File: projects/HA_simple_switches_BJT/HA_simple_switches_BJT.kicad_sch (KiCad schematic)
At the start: 16 parts

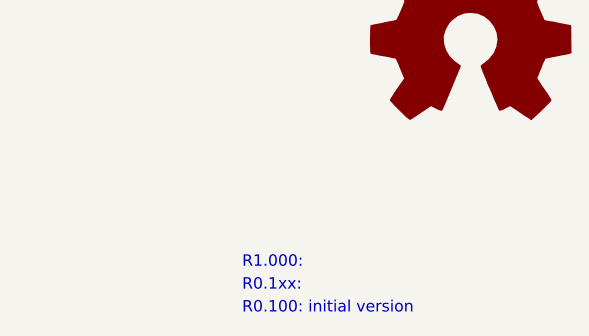
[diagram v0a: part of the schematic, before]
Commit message: v101 minor routing changes
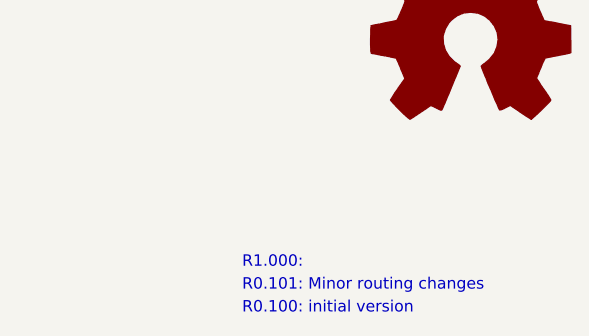
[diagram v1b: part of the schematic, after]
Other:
- note added: "R0.101: Minor routing changes"
- note removed: "R0.1xx:"

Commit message: snapshot
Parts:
- removed ?: (no value), symbol UH_Graphic:Logo_Open_Hardware_Small
- removed ? (x4): (no value), symbol UH_HA:TerminalBlock_3pin
- removed ?: (no value), symbol UH_HA:(C)UweHerting
- removed ?: (no value), symbol UH_HA:TerminalBlock_2pin
- removed ?: (no value), symbol UH_HA:https___github.com_uherting_MyKiCADRep
- added J1: Conn_01x02_Pin, Connector_PinHeader_2.54mm:PinHeader_1x02_P2.54mm_Vertical, symbol UH_HA:Conn_01x02_Pin
- added J2, J3, J4, J5: Conn_01x03_Pin, Connector_PinHeader_2.54mm:PinHeader_1x03_P2.54mm_Vertical, symbol UH_HA:Conn_01x03_Pin
- Q1, Q2, Q3: renamed from ?; value (none) -> MMBT3904; footprint (none) -> UH_HA:SOT-23
- R1, R2, R3: renamed from ?; value (none) -> 12k; footprint (none) -> Resistor_SMD:R_0805_2012Metric_Pad1.20x1.40mm_HandSolder
- T1: renamed from ?; value (none) -> HA_simple_switches_BJT; footprint (none) -> UH_HA:PCB_Name
- T4: renamed from ?; value (none) -> v0.102; footprint (none) -> UH_HA:PCB_Version
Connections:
- net +5V: now also J1.1 (Pin_1), J3.1 (Pin_1), J4.1 (Pin_1), J5.1 (Pin_1)
- net BJT_01: now also J3.2 (Pin_2)
- net BJT_02: now also J4.2 (Pin_2)
- net BJT_03: now also J5.2 (Pin_2)
- net GND: now also J1.2 (Pin_2), J3.3 (Pin_3), J4.3 (Pin_3), J5.3 (Pin_3)
- net GPIO_1: now also J2.1 (Pin_1)
- net GPIO_2: now also J2.2 (Pin_2)
- net GPIO_3: now also J2.3 (Pin_3)
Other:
- note added: "R0.102: Using pin headers instead of terminals"
- note removed: "R1.000:"
